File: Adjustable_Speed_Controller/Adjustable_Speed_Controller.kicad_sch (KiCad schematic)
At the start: 16 parts, among them J1 Screw_Terminal_01x02, J2 Jack-12V-DC, SW1 SW_SPDT, U1 IRLR7843, U3 NE555D

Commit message: Renamed the title
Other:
- company: (none) -> OSSEM
- title: (none) -> Adjustable Fan Controller
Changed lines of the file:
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@@
 	(generator_version "9.0")
 	(paper "A4")
+	(title_block
+		(title "Adjustable Fan Controller")
+		(date "2026-02-27")
+		(rev "1.0")
+		(company "OSSEM")
+	)
 	(rectangle
 		(start 132.08 63.5)

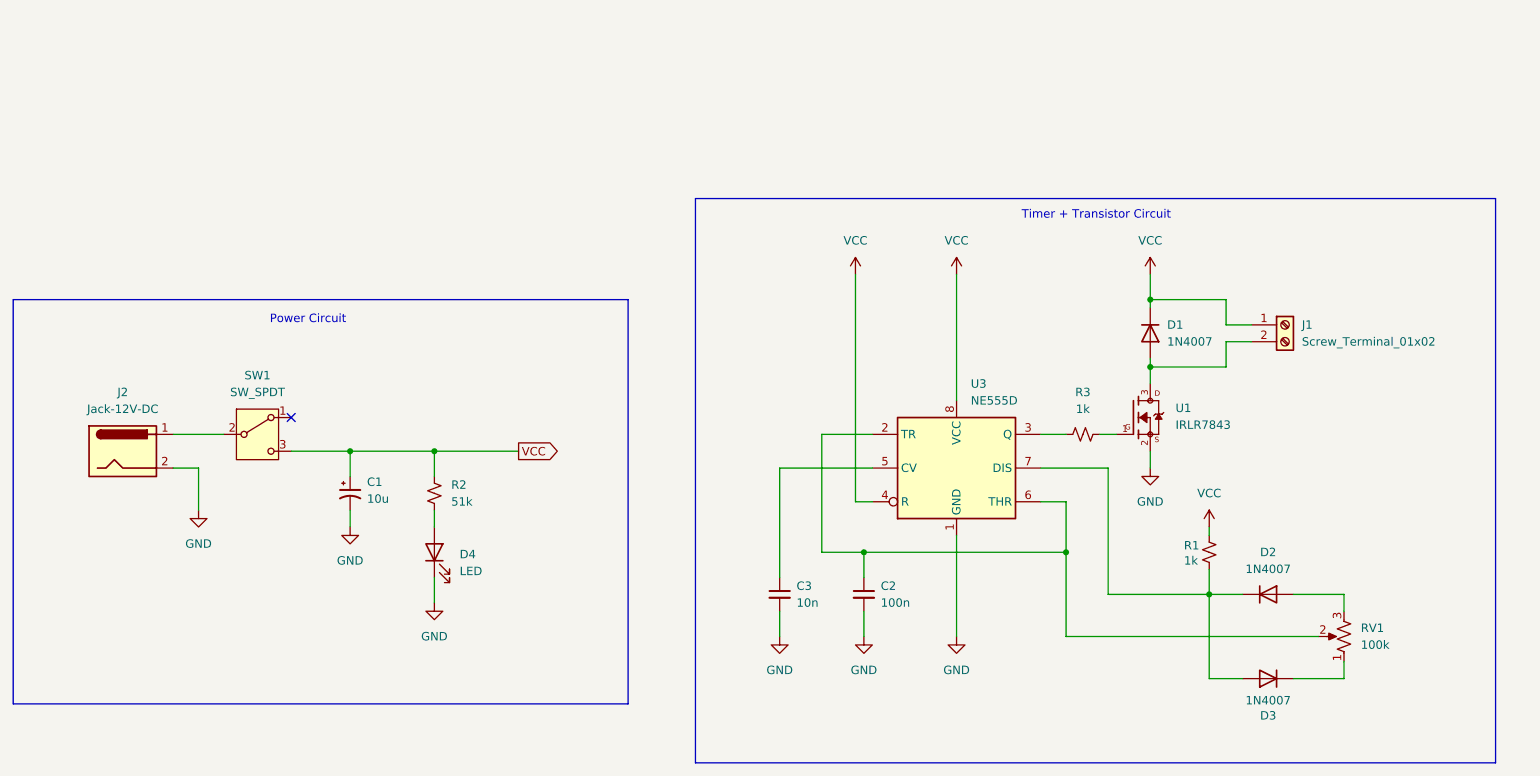
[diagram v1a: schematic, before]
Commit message: Replaced LR7843  footprint
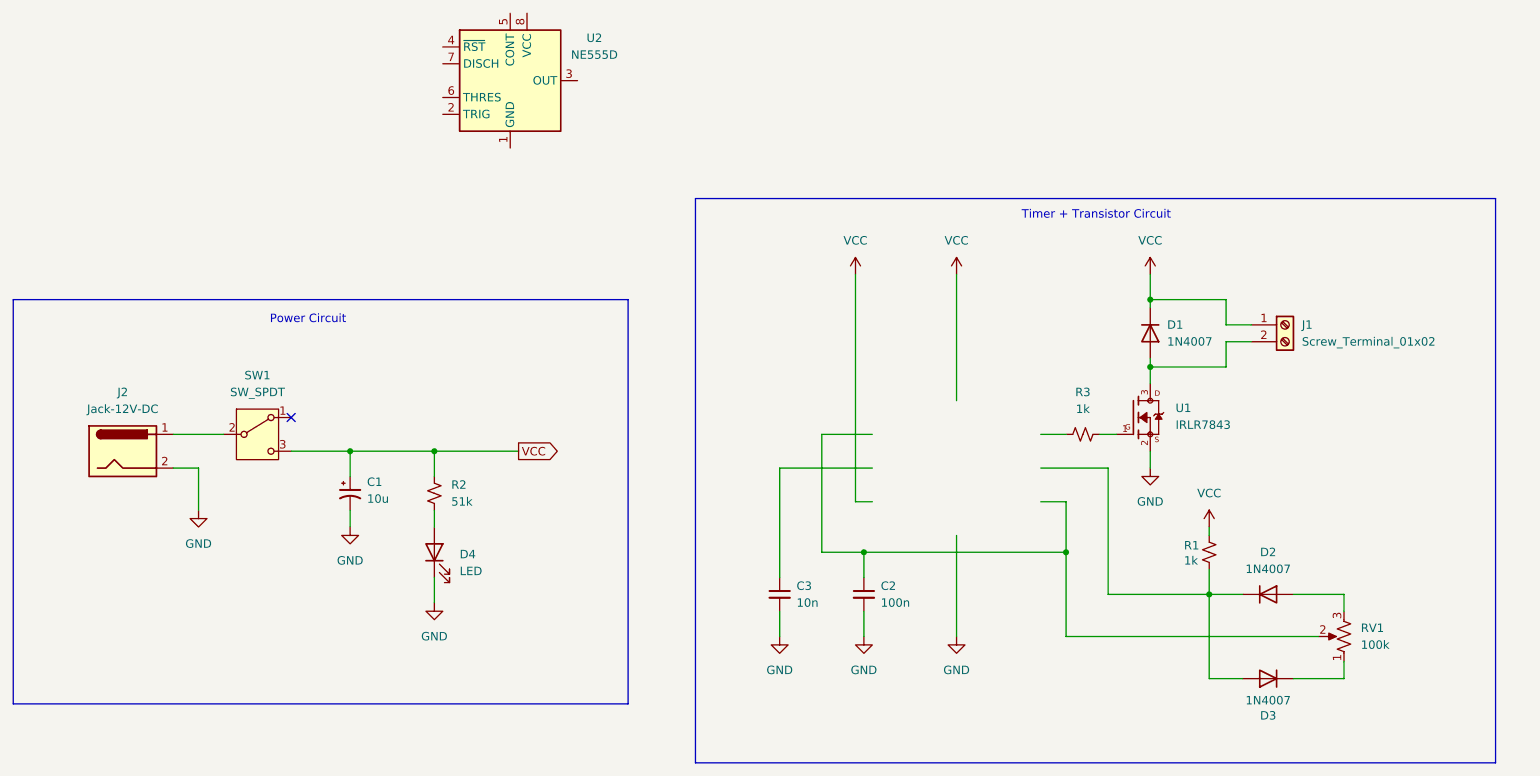
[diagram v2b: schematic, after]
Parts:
- removed U3: NE555D, Package_SO:SOIC-8_3.9x4.9mm_P1.27mm, symbol Timer:NE555D
- added U2: NE555D, Package_SO:SOIC-8_3.9x4.9mm_P1.27mm, symbol Timer:NE555D
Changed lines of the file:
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@@
-	)
-	(symbol
-		(lib_id "Timer:NE555D")
-		(at 171.45 104.14 0)
-		(unit 1)
-		(exclude_from_sim no)
-		(in_bom yes)
-		(on_board yes)
-		(dnp no)
-		(fields_autoplaced yes)
-		(property "Reference" "U3"
-			(at 173.5933 91.44 0)
-			(effects
-				(font
-					(size 1.27 1.27)
-				)
-				(justify left)
-			)
-		)
-		(property "Value" "NE555D"
-			(at 173.5933 93.98 0)
-			(effects
-				(font
-					(size 1.27 1.27)
-				)
-				(justify left)
-			)
-		)
-		(property "Footprint" "Package_SO:SOIC-8_3.9x4.9mm_P1.27mm"
-			(at 193.04 114.3 0)
-			(effects
-				(font
-					(size 1.27 1.27)
-				)
-				(hide yes)
-			)
-		)
-		(property "Datasheet" "http://www.ti.com/lit/ds/symlink/ne555.pdf"
-			(at 193.04 114.3 0)
-			(effects
-				(font
-					(size 1.27 1.27)
-				)
-				(hide yes)
-			)
-		)
-		(property "Description" "Precision Timers, 555 compatible, SOIC-8"
-			(at 171.45 104.14 0)
-			(effects
-				(font
-					(size 1.27 1.27)
-				)
-				(hide yes)
-			)
-		)
-		(pin "7"
-		)
-		(pin "6"
-		)
-		(pin "3"
-		)
-		(pin "4"
-		)
-		(pin "2"
-		)
-		(pin "8"
-		)
-		(pin "1"
-		)
-		(pin "5"
-		)
-		(instances
-			(project ""
-				(path "/fce28001-68a0-4ab4-89fe-ffc366d126a9"
-					(reference "U3")
-					(unit 1)
-				)
-			)
-		)
 	)
 	(symbol
@@
 	)
 	(symbol
+		(lib_id "IRLR7843:IRLR7843")
+		(at 198.12 96.52 0)
+		(unit 1)
+		(exclude_from_sim no)
+		(in_bom yes)
+		(on_board yes)
+		(dnp no)
+		(fields_autoplaced yes)
+		(property "Reference" "U1"
+			(at 204.47 95.1036 0)
+			(effects
+				(font
+					(size 1.27 1.27)
+				)
+				(justify left)
+			)
+		)
+		(property "Value" "IRLR7843"
+			(at 204.47 97.6436 0)
+			(effects
+				(font
+					(size 1.27 1.27)
+				)
+				(justify left)
+			)
+		)
+		(property "Footprint" "IRLR7843:TO252"
+			(at 198.12 96.52 0)
+			(effects
+				(font
+					(size 1.27 1.27)
+				)
+				(justify bottom)
+				(hide yes)
+			)
+		)
+		(property "Datasheet" ""
+			(at 198.12 96.52 0)
+			(effects
+				(font
+					(size 1.27 1.27)
+				)
+				(hide yes)
+			)
+		)
+		(property "Description" ""
+			(at 198.12 96.52 0)
+			(effects
+				(font
+					(size 1.27 1.27)
+				)
+				(hide yes)
+			)
+		)
+		(property "MF" "Infineon Technologies"
+			(at 198.12 96.52 0)
+			(effects
+				(font
+					(size 1.27 1.27)
+				)
+				(justify bottom)
+				(hide yes)
+			)
+		)
+		(property "Description_1" "N-Channel 30 V 161A (Tc) 140W (Tc) Surface Mount D-Pak"
+			(at 198.12 96.52 0)
+			(effects
+				(font
+					(size 1.27 1.27)
+				)
+				(justify bottom)
+				(hide yes)
+			)
+		)
+		(property "Package" "TO-252 Infineon"
+			(at 198.12 96.52 0)
+			(effects
+				(font
+					(size 1.27 1.27)
+				)
+				(justify bottom)
+				(hide yes)
+			)
+		)
+		(property "Price" "None"
+			(at 198.12 96.52 0)
+			(effects
+				(font
+					(size 1.27 1.27)
+				)
+				(justify bottom)
+				(hide yes)
+			)
+		)
+		(property "SnapEDA_Link" "https://www.snapeda.com/parts/IRLR7843/Infineon/view-part/?ref=snap"
+			(at 198.12 96.52 0)
+			(effects
+				(font
+					(size 1.27 1.27)
+				)
+				(justify bottom)
+				(hide yes)
+			)
+		)
+		(property "MP" "IRLR7843"
+			(at 198.12 96.52 0)
+			(effects
+				(font
+					(size 1.27 1.27)
+				)
+				(justify bottom)
+				(hide yes)
+			)
+		)
+		(property "Availability" "In Stock"
+			(at 198.12 96.52 0)
+			(effects
+				(font
+					(size 1.27 1.27)
+				)
+				(justify bottom)
+				(hide yes)
+			)
+		)
+		(property "Check_prices" "https://www.snapeda.com/parts/IRLR7843/Infineon/view-part/?ref=eda"
+			(at 198.12 96.52 0)
+			(effects
+				(font
+					(size 1.27 1.27)
+				)
+				(justify bottom)
+				(hide yes)
+			)
+		)
+		(pin "1"
+		)
+		(pin "3"
+		)
+		(pin "2"
+		)
+		(instances
+			(project ""
+				(path "/fce28001-68a0-4ab4-89fe-ffc366d126a9"
+					(reference "U1")
+					(unit 1)
+				)
+			)
+		)
+	)
+	(symbol
+		(lib_id "Timer:NE555D")
+		(at 104.14 45.72 0)
+		(unit 1)
+		(exclude_from_sim no)
+		(in_bom yes)
+		(on_board yes)
+		(dnp no)
+		(fields_autoplaced yes)
+		(property "Reference" "U2"
+			(at 116.84 39.2998 0)
+			(effects
+				(font
+					(size 1.27 1.27)
+				)
+			)
+		)
+		(property "Value" "NE555D"
+			(at 116.84 41.8398 0)
+			(effects
+				(font
+					(size 1.27 1.27)
+				)
+			)
+		)
+		(property "Footprint" "Package_SO:SOIC-8_3.9x4.9mm_P1.27mm"
+			(at 104.14 69.85 0)
+			(effects
+				(font
+					(size 1.27 1.27)
+				)
+				(hide yes)
+			)
+		)
+		(property "Datasheet" "http://www.ti.com/lit/ds/symlink/ne555.pdf"
+			(at 104.14 72.39 0)
+			(effects
+				(font
+					(size 1.27 1.27)
+				)
+				(hide yes)
+			)
+		)
+		(property "Description" "Precision Timers, 555 compatible, SOIC-8"
+			(at 104.14 67.31 0)
+			(effects
+				(font
+					(size 1.27 1.27)
+				)
+				(hide yes)
+			)
+		)
+		(pin "5"
+		)
+		(pin "2"
+		)
+		(pin "3"
+		)
+		(pin "4"
+		)
+		(pin "7"
+		)
+		(pin "8"
+		)
+		(pin "6"
+		)
+		(pin "1"
+		)
+		(instances
+			(project ""
+				(path "/fce28001-68a0-4ab4-89fe-ffc366d126a9"
+					(reference "U2")
+					(unit 1)
+				)
+			)
+		)
+	)
+	(symbol
 		(lib_id "Connector:Jack-DC")
 		(at 45.72 101.6 0)
@@
 					(unit 1)
 				)
-			)
-		)
-	)
-	(symbol
-		(lib_id "IRLR7843:IRLR7843")
-		(at 198.12 96.52 0)
-		(unit 1)
-		(exclude_from_sim no)
-		(in_bom yes)
-		(on_board yes)
-		(dnp no)
-		(fields_autoplaced yes)
-		(property "Reference" "U1"
-			(at 204.47 95.1036 0)
-			(effects
-				(font
-					(size 1.27 1.27)
-				)
-				(justify left)
-			)
-		)
-		(property "Value" "IRLR7843"
-			(at 204.47 97.6436 0)
-			(effects
-				(font
-					(size 1.27 1.27)
-				)
-				(justify left)
-			)
-		)
-		(property "Footprint" "IRLR7843:TO252"
-			(at 198.12 96.52 0)
-			(effects
-				(font
-					(size 1.27 1.27)
-				)
-				(justify bottom)
-				(hide yes)
-			)
-		)
-		(property "Datasheet" ""
-			(at 198.12 96.52 0)
-			(effects
-				(font
-					(size 1.27 1.27)
-				)
-				(hide yes)
-			)
-		)
-		(property "Description" ""
-			(at 198.12 96.52 0)
-			(effects
-				(font
-					(size 1.27 1.27)
-				)
-				(hide yes)
-			)
-		)
-		(property "MF" "Infineon Technologies"
-			(at 198.12 96.52 0)
-			(effects
-				(font
-					(size 1.27 1.27)
-				)
-				(justify bottom)
-				(hide yes)
-			)
-		)
-		(property "Description_1" "N-Channel 30 V 161A (Tc) 140W (Tc) Surface Mount D-Pak"
-			(at 198.12 96.52 0)
-			(effects
-				(font
-					(size 1.27 1.27)
-				)
-				(justify bottom)
-				(hide yes)
-			)
-		)
-		(property "Package" "TO-252 Infineon"
-			(at 198.12 96.52 0)
-			(effects
-				(font
-					(size 1.27 1.27)
-				)
-				(justify bottom)
-				(hide yes)
-			)
-		)
-		(property "Price" "None"
-			(at 198.12 96.52 0)
-			(effects
-				(font
-					(size 1.27 1.27)
-				)
-				(justify bottom)
-				(hide yes)
-			)
-		)
-		(property "SnapEDA_Link" "https://www.snapeda.com/parts/IRLR7843/Infineon/view-part/?ref=snap"
-			(at 198.12 96.52 0)
-			(effects
-				(font
-					(size 1.27 1.27)
-				)
-				(justify bottom)
-				(hide yes)
-			)
-		)
-		(property "MP" "IRLR7843"
-			(at 198.12 96.52 0)
-			(effects
-				(font
-					(size 1.27 1.27)
-				)
-				(justify bottom)
-				(hide yes)
-			)
-		)
-		(property "Availability" "In Stock"
-			(at 198.12 96.52 0)
-			(effects
-				(font
-					(size 1.27 1.27)
-				)
-				(justify bottom)
-				(hide yes)
-			)
-		)
-		(property "Check_prices" "https://www.snapeda.com/parts/IRLR7843/Infineon/view-part/?ref=eda"
-			(at 198.12 96.52 0)
-			(effects
-				(font
-					(size 1.27 1.27)
-				)
-				(justify bottom)
-				(hide yes)
-			)
-		)
-		(pin "3"
-		)
-		(pin "1"
-		)
-		(pin "2"
-		)
-		(instances
-			(project ""
-				(path "/fce28001-68a0-4ab4-89fe-ffc366d126a9"
-					(reference "U1")
-					(unit 1)
-				)

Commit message: Rev1.1 with new symbol
Kicad did a funny thing and decided to update its symbols and pinouts
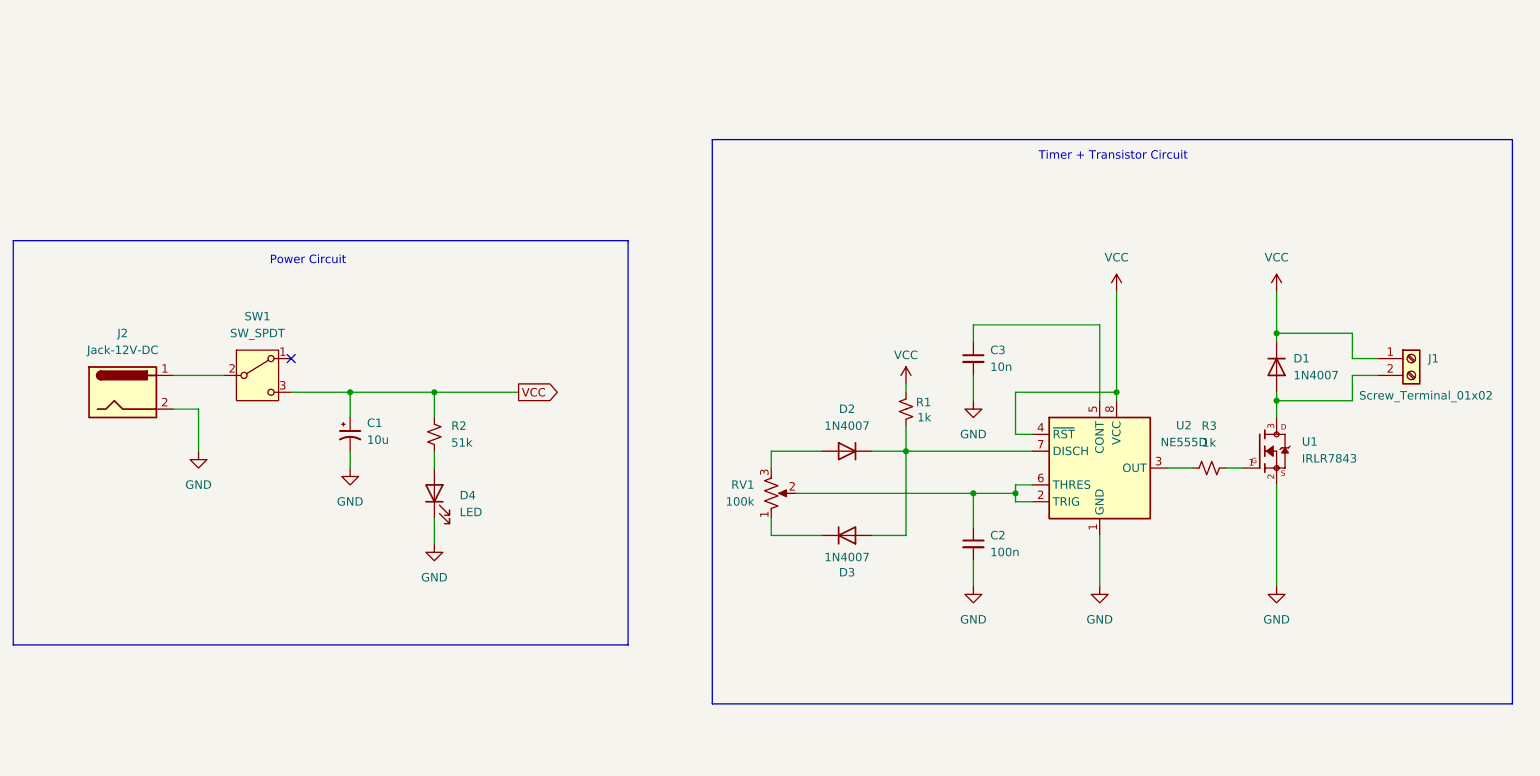
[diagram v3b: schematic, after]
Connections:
- net GND: now also U2.1 (GND)
- net VCC: now also U2.4 (~{RST}), U2.8 (VCC)
- net at C2.1, RV1.2: now also U2.2 (TRIG), U2.6 (THRES)
- net at R3.1: now also U2.3 (OUT)
- net at D2.1 (K), D3.2 (A), R1.1: now also U2.7 (DISCH)
- net at C3.1: now also U2.5 (CONT)
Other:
- moved on the sheet: C1, C2, C3, D1, D2, D3, D4, J1, J2, R1, R2, R3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
